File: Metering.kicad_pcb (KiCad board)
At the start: 2 copper layers, 100 x 50 mm, 25 parts, among them J1 Barrel_Jack_Switch, J10 Conn_01x15, J11 Conn_01x11, J2 Conn_01x15_Female, J3 Conn_01x15_Female, J4 Conn_01x15_Female, J5 Conn_01x15_Female, J6 Conn_01x15_Female, J7 Conn_01x15_Female, J8 Conn_01x15_Female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

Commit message: version 1.0
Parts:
- removed the REF** at (110.0, 59.0)
- removed the REF** at (110.0, 90.0)
- added ?: , , F.Cu at (114.0, 72.0)
- added G***: LOGO, w_logo:Logo_copper_CC-BY-NC-SA_10x3.6mm, F.Cu at (108.0, 74.9)
- added REF**: 1Pin, w_to:1pin, F.Cu at (110.0, 61.0)
- added REF**: 1Pin, w_to:1pin, F.Cu at (110.4, 88.0)
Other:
- board text added: "3V3"
- board text added: "GND"
- board text added: "Gerhard Bertelsmann Version 1.0 01/2019"
- board text added: "Imp"
- board text added: "Reed"
- board text added: "Vcc"

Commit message: add drills
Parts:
- added C3: 100nF, Capacitor_THT:C_Disc_D3.0mm_W2.0mm_P2.50mm, F.Cu at (174.1, 77.1)
- added R4: 1k, w_pth_resistors:RC03, F.Cu at (177.0, 75.8)
- R1: value 5k6 -> 10k
- moved R1 2.43 mm to (173.2, 69.6)
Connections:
- J3 pad 15: /GAS -> Net-(C3-Pad1)
- R1 pad 1: /GAS -> Net-(C3-Pad1)
- U1 pad 30: /GAS -> Net-(C3-Pad1)
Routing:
- net Net-(C3-Pad1): track 0.00 -> 124.5 mm
- net /GAS: track 109.6 -> 7.98 mm
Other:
- outline, holes or cut-outs redrawn
- board text added: "Gerhard Bertelsmann Version 1.1 02/2019"
- board text removed: "Gerhard Bertelsmann Version 1.0 01/2019"

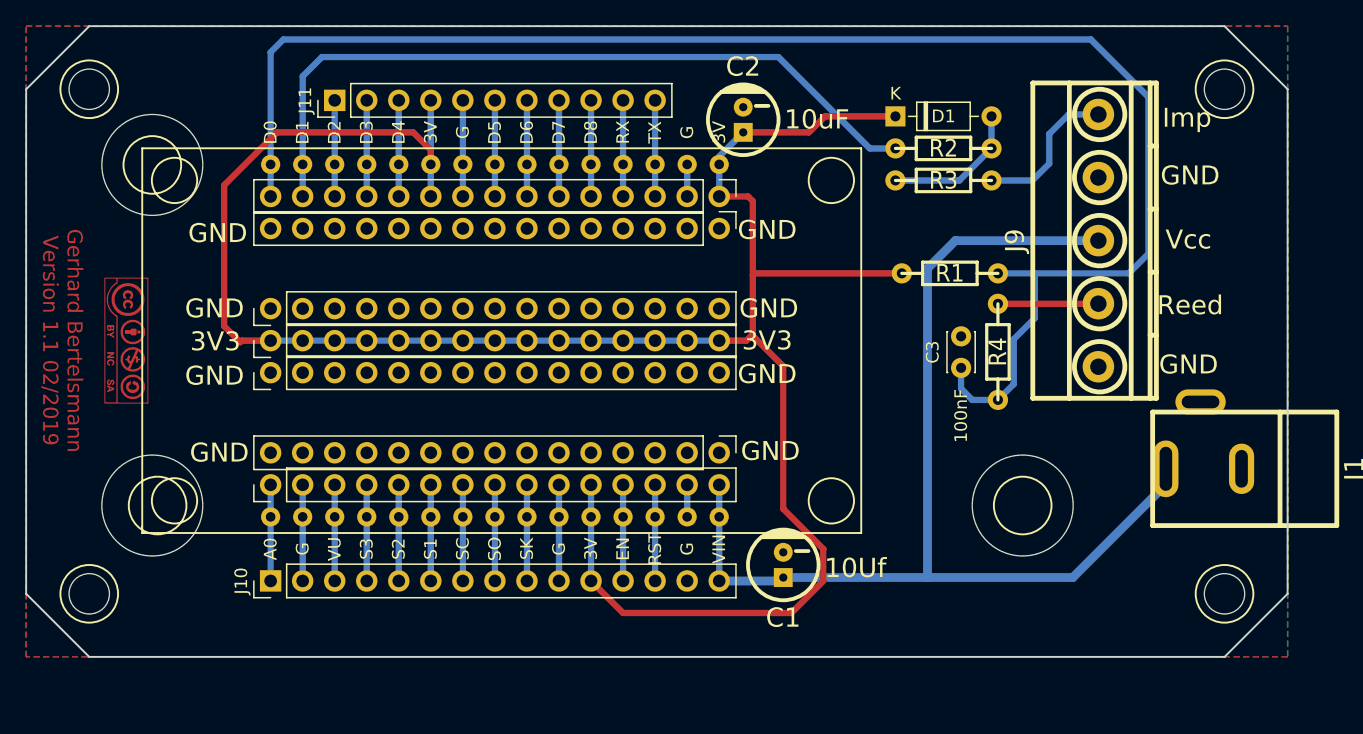
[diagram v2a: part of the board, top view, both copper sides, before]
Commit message: shorten board and use D2 instead of D0
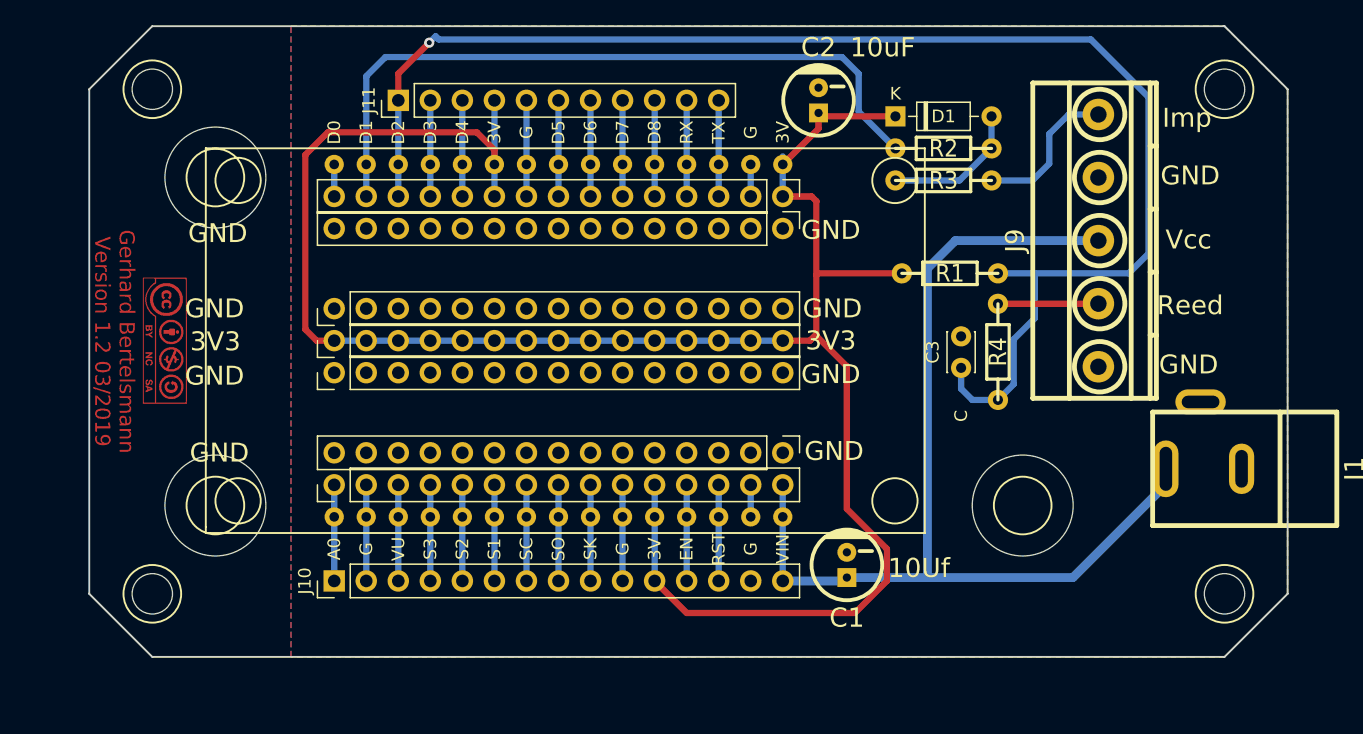
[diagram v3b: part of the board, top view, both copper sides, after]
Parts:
- C3: value 100nF -> C
- moved C2 6.16 mm to (162.8, 55.9)
- moved REF** 5.10 mm to (115.0, 62.0)
- moved U1 5.04 mm to (144.7, 74.9)
- moved J10 5.04 mm to (124.4, 94.0)
- moved J11 5.04 mm to (129.5, 55.9)
- moved J2 5.04 mm to (124.4, 86.4)
- moved J6 5.04 mm to (124.4, 72.4)
- moved J7 5.04 mm to (124.4, 77.5)
- moved J8 5.04 mm to (124.4, 74.9)
- moved C1 5.04 mm to (165.1, 92.7)
- moved J3 5.04 mm to (160.0, 63.5)
- moved J4 5.04 mm to (160.0, 66.0)
- moved J5 5.04 mm to (160.0, 83.8)
- moved REF** 5.00 mm to (110.0, 95.0)
- moved REF** 5.00 mm to (110.0, 55.0)
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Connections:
- C3 pad 1: Net-(C3-Pad1) -> /D2
- J3 pad 15: Net-(C3-Pad1) -> Net-(J3-Pad15)
- R1 pad 1: Net-(C3-Pad1) -> /D2
- R4 pad 2: Net-(C3-Pad1) -> /D2
- U1 pad 30: Net-(C3-Pad1) -> Net-(J3-Pad15)
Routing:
- net Net-(C3-Pad1): track 124.5 -> 0.00 mm
- net /D2: track 7.62 -> 113.6 mm, vias 0 -> 1
- net +3V3: track 175.0 -> 164.8 mm
- net +12V: track 86.4 -> 81.4 mm
- net Net-(J3-Pad14): track 60.1 -> 56.9 mm
- net Net-(J3-Pad15): track 0.00 -> 2.54 mm
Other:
- board size 100 x 50 mm -> 95 x 50 mm
- board text added: "Gerhard Bertelsmann Version 1.2 03/2019"
- board text removed: "Gerhard Bertelsmann Version 1.1 02/2019"
